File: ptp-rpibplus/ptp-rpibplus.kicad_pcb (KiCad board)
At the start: 2 copper layers, 65.5 x 56.6 mm, 9 parts, among them J1 RASPI_B+, J2 MODULE_HEADER, J3 MODULE_HEADER

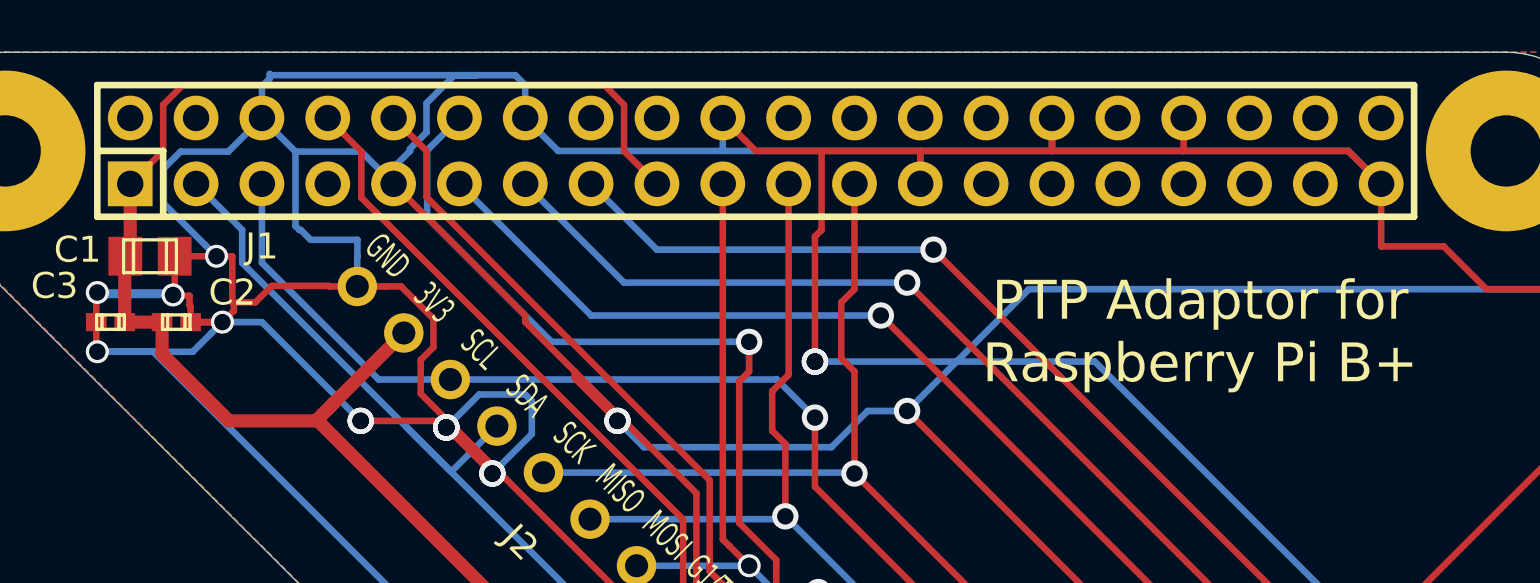
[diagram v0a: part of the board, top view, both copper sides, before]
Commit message: 10mil pour clear
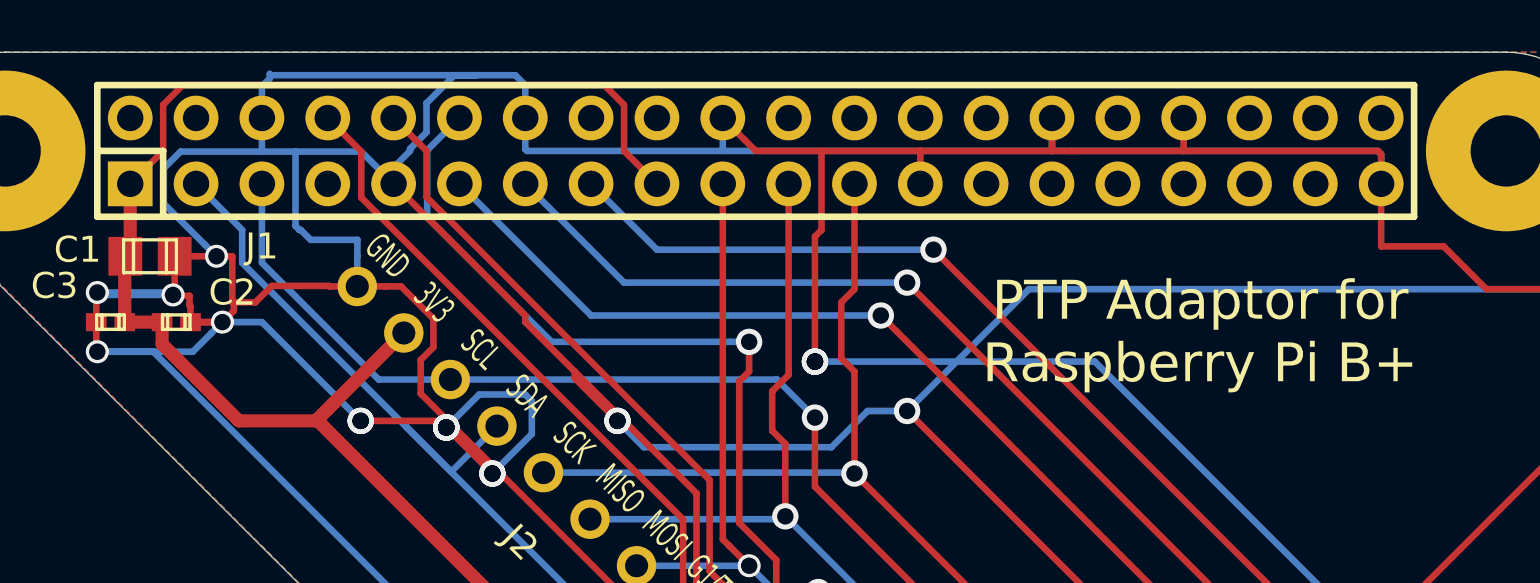
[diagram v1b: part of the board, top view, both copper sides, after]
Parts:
- turned H1 to 0 degrees
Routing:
- net GND: track 491.5 -> 493.7 mm
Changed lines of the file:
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@@
     (thickness 1.6)
     (drawings 84)
-    (tracks 305)
+    (tracks 310)
     (zones 0)
     (modules 9)
@@
   )
   (module parts:HOLE-2.75mm-6.2mm (layer F.Cu)
-    (at 98.044 80.01 90)
-    (fp_text reference H1 (at 0 -5.08 90) (layer F.SilkS) hide
+    (at 98.044 80.01)
+    (fp_text reference H1 (at 0 -5.08) (layer F.SilkS) hide
       (effects (font (size 1 1) (thickness 0.15)))
     )
-    (fp_text value HOLE (at 0 5.08 90) (layer F.SilkS) hide
+    (fp_text value HOLE (at 0 5.08) (layer F.SilkS) hide
       (effects (font (size 1 1) (thickness 0.15)))
     )
-    (pad "" np_thru_hole circle (at 0 0 90) (size 6.2 6.2) (drill 2.75) (layers *.Cu *.Mask F.SilkS))
+    (pad "" np_thru_hole circle (at 0 0) (size 6.2 6.2) (drill 2.75) (layers *.Cu *.Mask F.SilkS))
   )
   (module parts:HOLE-2.75mm-6.2mm (layer F.Cu)
@@
   )
   (segment (start 128.016 106.68) (end 111.76 90.424) (width 0.254) (layer Dwgs.User) (net 0))
+  (segment (start 121.92 80.01) (end 123.19 81.28) (width 0.254) (layer F.Cu) (net 1) (status 20))
+  (segment (start 121.92 78.232) (end 121.92 80.01) (width 0.254) (layer F.Cu) (net 1))
+  (segment (start 104.902 77.47) (end 121.158 77.47) (width 0.254) (layer F.Cu) (net 1))
+  (segment (start 104.14 78.232) (end 104.902 77.47) (width 0.254) (layer F.Cu) (net 1))
+  (segment (start 121.158 77.47) (end 121.92 78.232) (width 0.254) (layer F.Cu) (net 1))
+  (segment (start 104.14 80.01) (end 104.14 78.232) (width 0.254) (layer F.Cu) (net 1))
+  (segment (start 102.87 81.28) (end 104.14 80.01) (width 0.254) (layer F.Cu) (net 1) (status 10))
   (segment (start 110.706221 89.751221) (end 110.033442 90.424) (width 0.508) (layer F.Cu) (net 1))
-  (segment (start 110.033442 90.424) (end 106.68 90.424) (width 0.508) (layer F.Cu) (net 1))
-  (segment (start 106.68 90.424) (end 104.09936 87.84336) (width 0.508) (layer F.Cu) (net 1))
-  (segment (start 104.09936 87.84336) (end 104.09936 86.614) (width 0.508) (layer F.Cu) (net 1))
+  (segment (start 110.033442 90.424) (end 107.061 90.424) (width 0.508) (layer F.Cu) (net 1))
+  (segment (start 107.061 90.424) (end 104.09936 87.46236) (width 0.508) (layer F.Cu) (net 1))
+  (segment (start 104.09936 87.46236) (end 104.09936 86.614) (width 0.508) (layer F.Cu) (net 1))
   (segment (start 135.064821 108.674221) (end 128.359221 108.674221) (width 0.508) (layer F.Cu) (net 1))
   (segment (start 128.359221 108.674221) (end 110.071221 90.386221) (width 0.508) (layer F.Cu) (net 1))
@@
   (segment (start 102.87 83.8835) (end 102.6795 84.074) (width 0.508) (layer F.Cu) (net 1) (status 30))
   (segment (start 102.87 81.28) (end 102.87 83.8835) (width 0.508) (layer F.Cu) (net 1) (status 30))
-  (segment (start 102.87 81.28) (end 104.14 80.01) (width 0.254) (layer F.Cu) (net 1) (status 10))
-  (segment (start 104.14 80.01) (end 104.14 78.232) (width 0.254) (layer F.Cu) (net 1))
-  (segment (start 104.14 78.232) (end 104.902 77.47) (width 0.254) (layer F.Cu) (net 1))
-  (segment (start 104.902 77.47) (end 121.158 77.47) (width 0.254) (layer F.Cu) (net 1))
-  (segment (start 121.158 77.47) (end 121.92 78.232) (width 0.254) (layer F.Cu) (net 1))
-  (segment (start 121.92 78.232) (end 121.92 80.01) (width 0.254) (layer F.Cu) (net 1))
-  (segment (start 121.92 80.01) (end 123.19 81.28) (width 0.254) (layer F.Cu) (net 1) (status 20))
   (segment (start 102.65664 86.614) (end 102.65664 84.09686) (width 0.508) (layer F.Cu) (net 1))
   (segment (start 104.09936 86.614) (end 102.65664 86.614) (width 0.508) (layer F.Cu) (net 1))
   (segment (start 102.65664 84.09686) (end 102.6795 84.074) (width 0.508) (layer F.Cu) (net 1))
   (segment (start 113.424021 87.033421) (end 110.706221 89.751221) (width 0.508) (layer F.Cu) (net 1))
+  (segment (start 107.95 80.01) (end 107.924601 80.035399) (width 0.254) (layer B.Cu) (net 2))
+  (segment (start 107.924601 80.035399) (end 104.812591 80.035399) (width 0.254) (layer B.Cu) (net 2))
+  (segment (start 104.812591 80.035399) (end 104.165399 80.682591) (width 0.254) (layer B.Cu) (net 2))
+  (segment (start 104.165399 80.682591) (end 104.165399 82.042867) (width 0.254) (layer B.Cu) (net 2))
+  (segment (start 104.165399 82.042867) (end 105.752033 83.629501) (width 0.254) (layer B.Cu) (net 2))
+  (segment (start 105.752033 83.629501) (end 106.196532 84.074) (width 0.254) (layer B.Cu) (net 2))
+  (segment (start 109.245399 80.035399) (end 107.975399 80.035399) (width 0.254) (layer B.Cu) (net 2))
+  (segment (start 107.975399 80.035399) (end 107.95 80.01) (width 0.254) (layer B.Cu) (net 2))
+  (segment (start 107.95 80.01) (end 107.95 78.74) (width 0.254) (layer B.Cu) (net 2))
+  (segment (start 133.35 80.01) (end 118.1735 80.01) (width 0.254) (layer B.Cu) (net 2))
+  (segment (start 118.1735 80.01) (end 118.11 79.9465) (width 0.254) (layer B.Cu) (net 2))
+  (segment (start 118.11 79.9465) (end 118.11 78.74) (width 0.254) (layer B.Cu) (net 2))
+  (segment (start 151.13 81.28) (end 151.13 80.137) (width 0.254) (layer B.Cu) (net 2))
+  (segment (start 151.13 80.137) (end 151.003 80.01) (width 0.254) (layer B.Cu) (net 2))
+  (segment (start 151.003 80.01) (end 143.51 80.01) (width 0.254) (layer B.Cu) (net 2))
+  (segment (start 151.13 81.28) (end 151.13 80.137) (width 0.254) (layer F.Cu) (net 2))
+  (segment (start 151.13 80.137) (end 151.003 80.01) (width 0.254) (layer F.Cu) (net 2))
+  (segment (start 151.003 80.01) (end 143.527191 80.01) (width 0.254) (layer F.Cu) (net 2))
+  (segment (start 143.527191 80.01) (end 143.501792 79.984601) (width 0.254) (layer F.Cu) (net 2))
   (via (at 143.002 101.346) (size 1.016) (drill 0.635) (layers F.Cu B.Cu) (net 2))
   (segment (start 143.002 101.346) (end 139.573 101.346) (width 0.254) (layer B.Cu) (net 2))
@@
   (segment (start 126.104617 109.474) (end 146.304 129.673383) (width 0.254) (layer F.Cu) (net 2))
   (segment (start 146.304 129.673383) (end 146.304 130.302) (width 0.254) (layer F.Cu) (net 2))
-  (segment (start 151.13 81.28) (end 149.86 80.01) (width 0.254) (layer B.Cu) (net 2) (status 10))
-  (segment (start 149.86 80.01) (end 143.51 80.01) (width 0.254) (layer B.Cu) (net 2))
   (segment (start 143.51 80.01) (end 143.51 78.74) (width 0.254) (layer B.Cu) (net 2) (status 20))
   (segment (start 138.43 80.01) (end 138.43 78.74) (width 0.254) (layer B.Cu) (net 2) (status 20))
   (segment (start 133.35 81.28) (end 133.35 80.01) (width 0.254) (layer B.Cu) (net 2) (status 10))
-  (segment (start 109.245399 80.035399) (end 107.95 78.74) (width 0.254) (layer B.Cu) (net 2) (status 20))
   (segment (start 111.785399 80.035399) (end 109.245399 80.035399) (width 0.254) (layer B.Cu) (net 2))
   (segment (start 113.03 81.28) (end 111.785399 80.035399) (width 0.254) (layer B.Cu) (net 2) (status 10))
@@
   (segment (start 143.476393 80.01) (end 138.474201 80.01) (width 0.254) (layer F.Cu) (net 2))
   (segment (start 143.501792 79.984601) (end 143.476393 80.01) (width 0.254) (layer F.Cu) (net 2))
-  (segment (start 143.527191 80.01) (end 143.501792 79.984601) (width 0.254) (layer F.Cu) (net 2))
-  (segment (start 149.86 80.01) (end 143.527191 80.01) (width 0.254) (layer F.Cu) (net 2))
-  (segment (start 151.13 81.28) (end 149.86 80.01) (width 0.254) (layer F.Cu) (net 2))
   (segment (start 126.580671 79.590671) (end 125.73 78.74) (width 0.254) (layer F.Cu) (net 2))
   (segment (start 127 80.01) (end 126.580671 79.590671) (width 0.254) (layer F.Cu) (net 2))
   (segment (start 133.35 81.28) (end 133.35 80.01) (width 0.254) (layer F.Cu) (net 2))
-  (segment (start 119.38 80.01) (end 118.11 78.74) (width 0.254) (layer B.Cu) (net 2))
-  (segment (start 133.35 80.01) (end 119.38 80.01) (width 0.254) (layer B.Cu) (net 2))
   (segment (start 105.19664 86.01075) (end 105.156 85.97011) (width 0.254) (layer F.Cu) (net 2))
   (segment (start 105.19664 86.614) (end 105.19664 86.01075) (width 0.254) (layer F.Cu) (net 2))
@@
   (segment (start 116.235198 77.089) (end 117.729 77.089) (width 0.254) (layer B.Cu) (net 2))
   (segment (start 108.301372 77.089) (end 116.235198 77.089) (width 0.254) (layer B.Cu) (net 2))
-  (segment (start 105.752033 83.629501) (end 106.196532 84.074) (width 0.254) (layer B.Cu) (net 2))
-  (segment (start 104.165399 82.042867) (end 105.752033 83.629501) (width 0.254) (layer B.Cu) (net 2))
-  (segment (start 104.812591 80.035399) (end 104.165399 80.682591) (width 0.254) (layer B.Cu) (net 2))
-  (segment (start 106.654601 80.035399) (end 104.812591 80.035399) (width 0.254) (layer B.Cu) (net 2))
-  (segment (start 104.165399 80.682591) (end 104.165399 82.042867) (width 0.254) (layer B.Cu) (net 2))
-  (segment (start 107.95 78.74) (end 106.654601 80.035399) (width 0.254) (layer B.Cu) (net 2))
   (segment (start 107.188 83.058) (end 105.41 81.28) (width 0.254) (layer B.Cu) (net 4) (status 20))
   (segment (start 107.188 84.328) (end 107.188 83.058) (width 0.254) (layer B.Cu) (net 4))
@@
     (connect_pads (clearance 0.254))
     (min_thickness 0.254)
-    (fill yes (arc_segments 16) (thermal_gap 0.508) (thermal_bridge_width 0.508))
+    (fill yes (arc_segments 16) (thermal_gap 0.254) (thermal_bridge_width 0.508))
     (polygon
       (pts
@@
     (connect_pads (clearance 0.254))
     (min_thickness 0.254)
-    (fill yes (arc_segments 16) (thermal_gap 0.508) (thermal_bridge_width 0.508))
+    (fill yes (arc_segments 16) (thermal_gap 0.254) (thermal_bridge_width 0.508))
     (polygon
       (pts

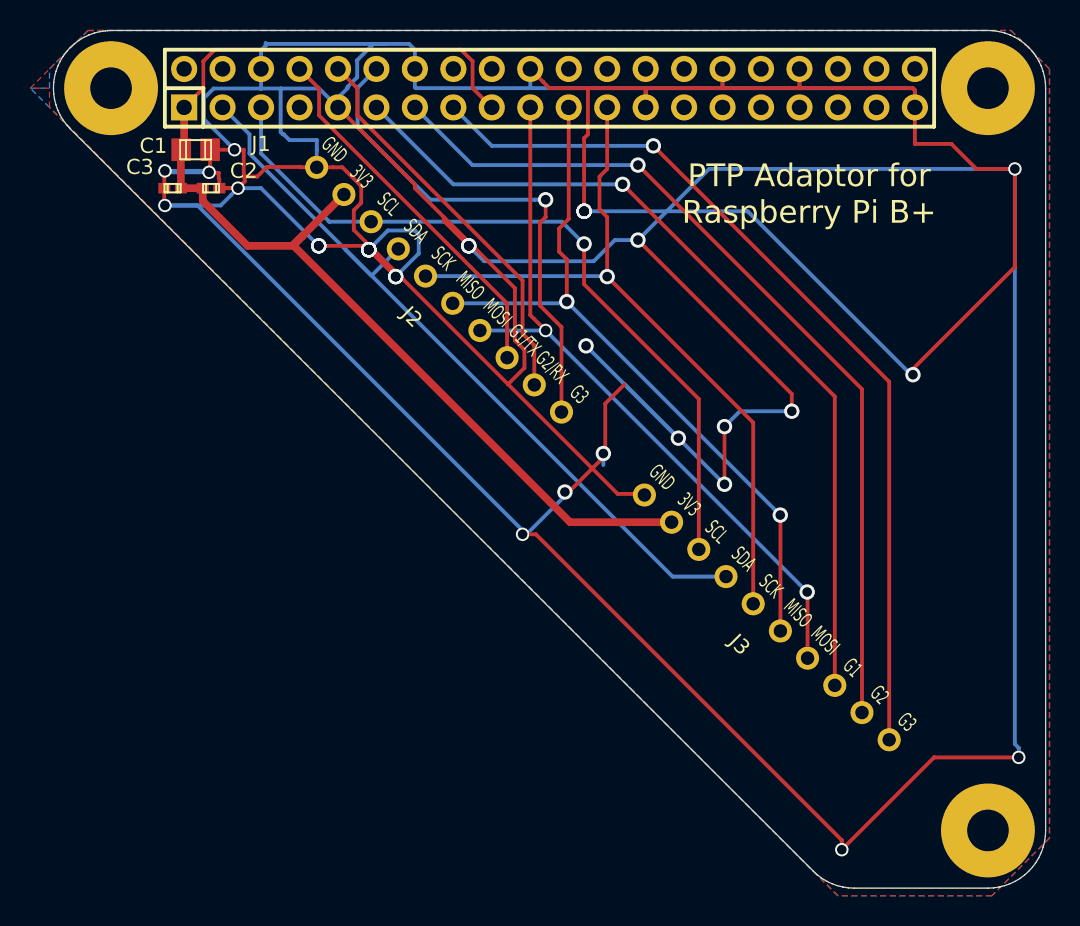
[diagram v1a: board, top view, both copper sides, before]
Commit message: drc pass ...stupid vias
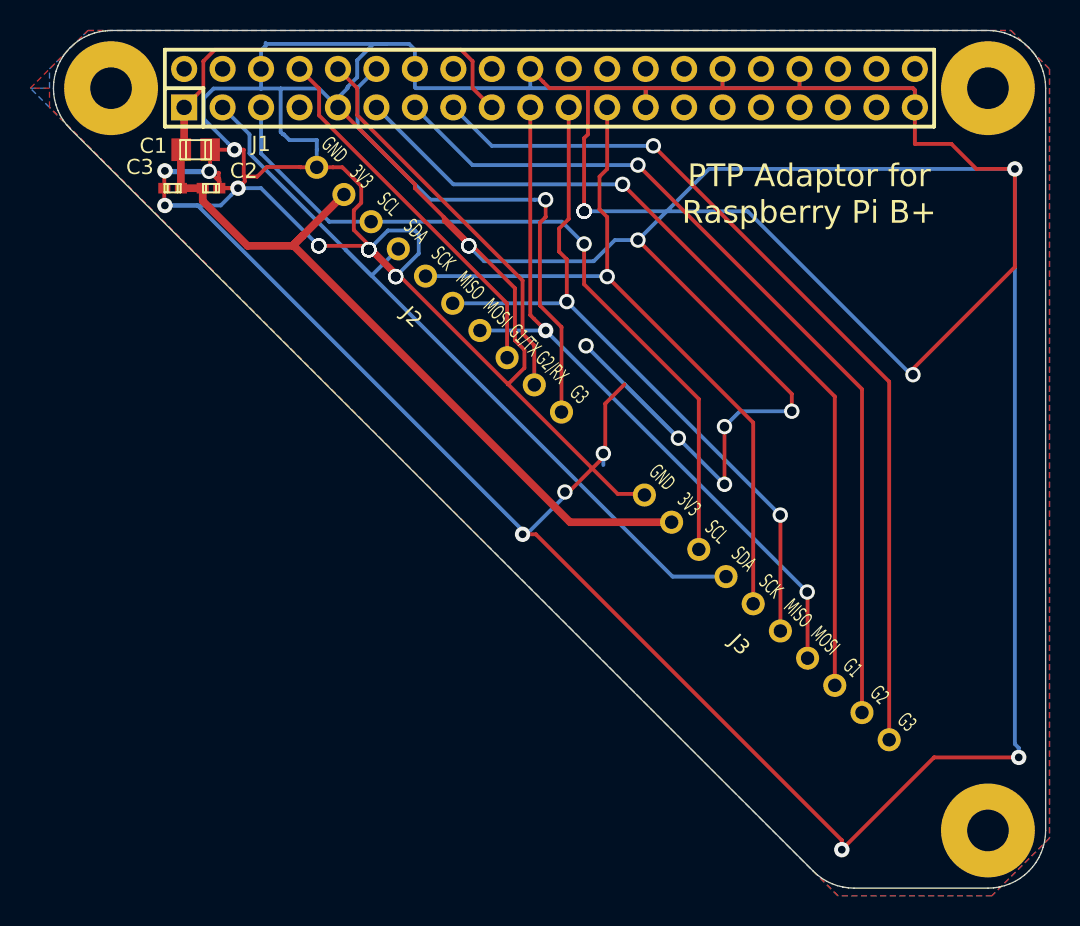
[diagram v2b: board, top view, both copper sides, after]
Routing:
- net GND: track 493.7 -> 495.1 mm
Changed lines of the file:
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@@
     (thickness 1.6)
     (drawings 84)
-    (tracks 310)
+    (tracks 312)
     (zones 0)
     (modules 9)
@@
   (segment (start 102.65664 84.09686) (end 102.6795 84.074) (width 0.508) (layer F.Cu) (net 1))
   (segment (start 113.424021 87.033421) (end 110.706221 89.751221) (width 0.508) (layer F.Cu) (net 1))
+  (segment (start 105.19664 86.614) (end 105.19664 86.175716) (width 0.254) (layer F.Cu) (net 2))
+  (segment (start 105.19664 86.175716) (end 104.524071 85.503147) (width 0.254) (layer F.Cu) (net 2))
+  (via (at 104.524071 85.503147) (size 1.016) (drill 0.635) (layers F.Cu B.Cu) (net 2))
   (segment (start 107.95 80.01) (end 107.924601 80.035399) (width 0.254) (layer B.Cu) (net 2))
   (segment (start 107.924601 80.035399) (end 104.812591 80.035399) (width 0.254) (layer B.Cu) (net 2))
@@
   (segment (start 137.541 85.344) (end 132.842 90.043) (width 0.254) (layer B.Cu) (net 2))
   (via (at 132.842 90.043) (size 1.016) (drill 0.635) (layers F.Cu B.Cu) (net 2))
-  (via (at 125.222 109.474) (size 0.889) (drill 0.635) (layers F.Cu B.Cu) (net 2))
+  (via (at 125.222 109.474) (size 1.016) (layers F.Cu B.Cu) (net 2))
   (segment (start 125.222 109.474) (end 125.222 109.22) (width 0.254) (layer B.Cu) (net 2))
   (segment (start 125.222 109.22) (end 103.759 87.757) (width 0.254) (layer B.Cu) (net 2))
@@
   (segment (start 104.5845 85.5345) (end 104.5845 84.074) (width 0.254) (layer F.Cu) (net 2))
   (segment (start 104.521 85.598) (end 104.5845 85.5345) (width 0.254) (layer F.Cu) (net 2))
-  (via (at 104.522016 85.566614) (size 0.889) (drill 0.635) (layers F.Cu B.Cu) (net 2))
-  (via (at 106.196532 84.074) (size 0.889) (drill 0.635) (layers F.Cu B.Cu) (net 2))
+  (via (at 106.196532 84.074) (size 1.016) (layers F.Cu B.Cu) (net 2))
   (segment (start 104.5845 84.074) (end 106.196532 84.074) (width 0.254) (layer F.Cu) (net 2))
   (segment (start 106.196532 84.074) (end 106.807 84.074) (width 0.254) (layer F.Cu) (net 2))
-  (via (at 101.6 87.757) (size 0.889) (drill 0.635) (layers F.Cu B.Cu) (net 2))
+  (via (at 101.6 87.757) (size 1.016) (layers F.Cu B.Cu) (net 2))
   (segment (start 101.55936 86.614) (end 101.55936 87.71636) (width 0.254) (layer F.Cu) (net 2))
   (segment (start 101.55936 87.71636) (end 101.6 87.757) (width 0.254) (layer F.Cu) (net 2))
-  (via (at 101.6 85.471) (size 0.889) (drill 0.635) (layers F.Cu B.Cu) (net 2))
+  (via (at 101.6 85.471) (size 1.016) (layers F.Cu B.Cu) (net 2))
   (segment (start 104.426402 85.471) (end 101.6 85.471) (width 0.254) (layer B.Cu) (net 2))
   (segment (start 104.522016 85.566614) (end 101.695614 85.566614) (width 0.254) (layer B.Cu) (net 2))
@@
   (segment (start 105.19664 86.614) (end 106.426 86.614) (width 0.254) (layer F.Cu) (net 2))
   (segment (start 106.614811 86.614) (end 106.426 86.614) (width 0.254) (layer F.Cu) (net 2))
-  (via (at 106.426 86.614) (size 0.889) (drill 0.635) (layers F.Cu B.Cu) (net 2))
+  (via (at 106.426 86.614) (size 1.016) (layers F.Cu B.Cu) (net 2))
   (segment (start 105.283 86.614) (end 106.426 86.614) (width 0.254) (layer F.Cu) (net 2))
   (segment (start 106.807 85.852) (end 106.870499 85.915499) (width 0.254) (layer F.Cu) (net 2))
@@
   (segment (start 113.319611 85.237369) (end 112.705599 85.237369) (width 0.254) (layer F.Cu) (net 2))
   (segment (start 133.268769 106.878169) (end 133.1976 106.807) (width 0.254) (layer F.Cu) (net 2))
-  (via (at 146.304 130.302) (size 0.889) (drill 0.635) (layers F.Cu B.Cu) (net 2))
+  (via (at 146.304 130.302) (size 1.016) (layers F.Cu B.Cu) (net 2))
   (segment (start 146.304 130.302) (end 152.4 124.206) (width 0.254) (layer F.Cu) (net 2))
-  (via (at 157.988 124.206) (size 0.889) (drill 0.635) (layers F.Cu B.Cu) (net 2))
+  (via (at 157.988 124.206) (size 1.016) (layers F.Cu B.Cu) (net 2))
   (segment (start 152.4 124.206) (end 157.988 124.206) (width 0.254) (layer F.Cu) (net 2))
   (segment (start 157.988 123.577383) (end 157.734 123.323383) (width 0.254) (layer B.Cu) (net 2))
   (segment (start 157.988 124.206) (end 157.988 123.577383) (width 0.254) (layer B.Cu) (net 2))
-  (via (at 157.734 85.344) (size 0.889) (drill 0.635) (layers F.Cu B.Cu) (net 2))
+  (via (at 157.734 85.344) (size 1.016) (layers F.Cu B.Cu) (net 2))
   (segment (start 157.734 123.323383) (end 157.734 85.344) (width 0.254) (layer B.Cu) (net 2))
   (segment (start 155.194 85.344) (end 153.543 83.693) (width 0.254) (layer F.Cu) (net 2))
@@
   (segment (start 122.404277 96.013677) (end 126.747677 96.013677) (width 0.254) (layer B.Cu) (net 16) (status 10))
   (segment (start 126.747677 96.013677) (end 144.018 113.284) (width 0.254) (layer B.Cu) (net 16))
-  (via (at 126.747677 96.013677) (size 0.889) (drill 0.635) (layers F.Cu B.Cu) (net 16))
+  (via (at 126.747677 96.013677) (size 1.016) (layers F.Cu B.Cu) (net 16))
   (segment (start 128.143 94.107) (end 142.24 108.204) (width 0.254) (layer B.Cu) (net 17))
   (via (at 128.143 94.107) (size 1.016) (drill 0.635) (layers F.Cu B.Cu) (net 17))
